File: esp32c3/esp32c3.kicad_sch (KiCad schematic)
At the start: 24 parts, among them J1 Conn_01x06, SW1 FLASH, SW2 RESET, U1 ESP32-C3-WROOM-02, U2 AHT10, U3 VEML7700, U4 LIS2DH, U5 HX6306

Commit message: add wake up, voltage measurement
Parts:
- removed C11: 10uF, Capacitor_SMD:C_0603_1608Metric, symbol Device:C_Small
- removed C3: 0.1uF, Capacitor_SMD:C_0603_1608Metric_Pad1.05x0.95mm_HandSolder, symbol e-tinkers-esp32-c3-rescue:C-Device
- removed C5: 1uF, Capacitor_SMD:C_0603_1608Metric_Pad1.05x0.95mm_HandSolder, symbol e-tinkers-esp32-c3-rescue:C-Device
- removed SW1: FLASH, e-tinkers:SW_TS-1185-X-X, symbol e-tinkers-esp32-c3-rescue:SW_Push-Switch
- added J1: A1501WR-S-2P, symbol esp32c3-altium-import:A1501WR-S-2P
- added R4: 1K, Resistor_SMD:R_0603_1608Metric_Pad1.05x0.95mm_HandSolder, symbol e-tinkers-esp32-c3-rescue:R-Device
- C4: value 0.1uF -> 10uF
- R1: value 10k -> 12k
- R5: value 12k -> 2k
- SW1: renamed from SW2; value RESET -> wake up
- renumbered J1 to J2, R4 to R6
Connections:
- net +3V3: now also R4.1; no longer R5.2
- net EN: now also J2.6 (Pin_6); no longer SW1.2
- net GND: now also R5.2
- net IO1: now also U4.6 (INT1)
- net IO2: now also R5.1, R4.2
- net IO4: now also SW1.2
- net IO10: no longer names the net of U1.10 (IO10)
- net IO18: no longer names the net of U1.13 (IO18)
- net IO19: no longer names the net of U1.14 (IO19)
- net IO3: no longer names the net of U1.15 (IO3)
- net IO5: no longer names the net of U1.4 (IO5)
- net IO6: no longer names the net of U1.5 (IO6)
- net IO7: no longer names the net of U1.6 (IO7)
- no-connect marks 2 -> 8
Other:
- moved on the sheet: C4, R1, SW1

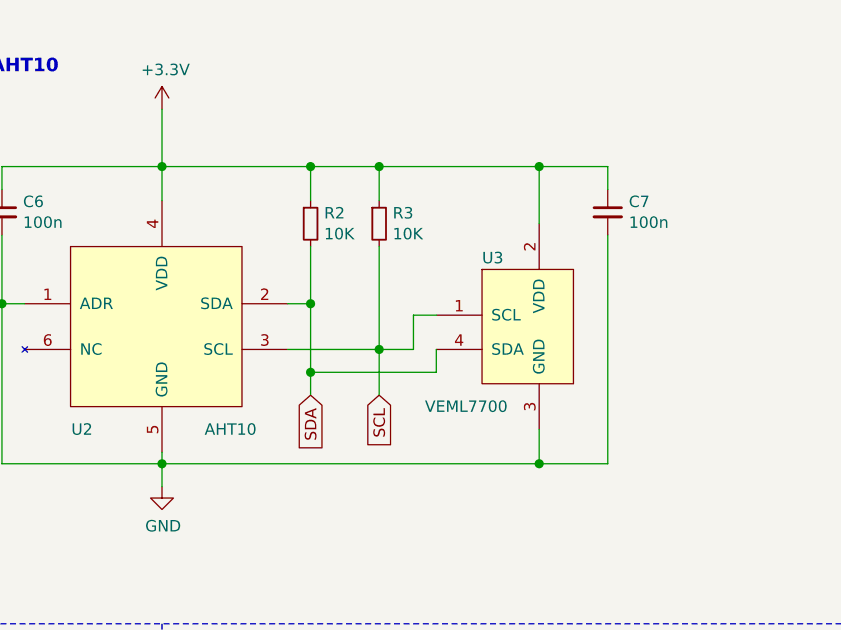
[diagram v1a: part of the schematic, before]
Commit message: delete VEML7700
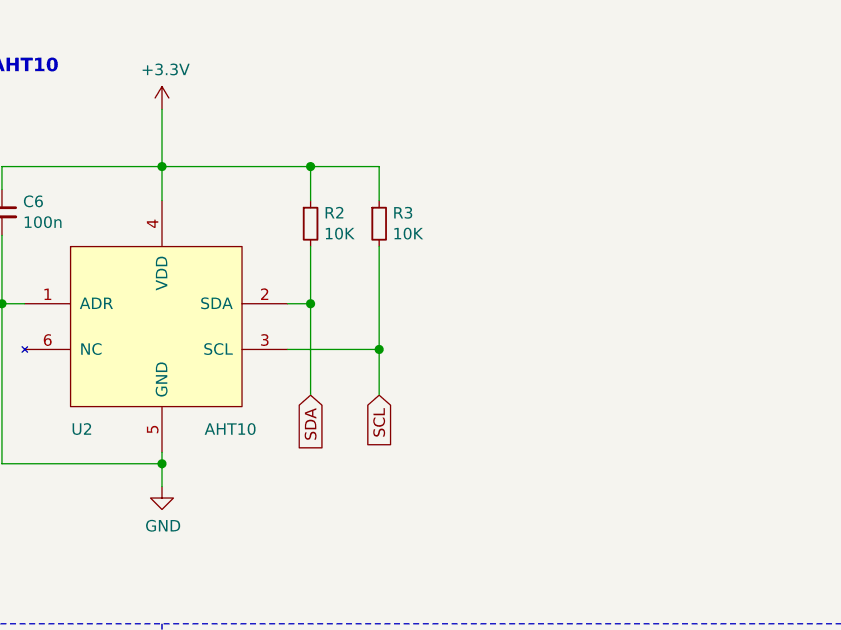
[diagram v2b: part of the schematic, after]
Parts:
- removed C7: 100n, Capacitor_SMD:C_0805_2012Metric, symbol ESP-AHT10-Extra-rescue:C_Small-Device
- removed U3: VEML7700, CPB:VEML7700, symbol ESP-AHT10-Extra-rescue:VEML7700-VEML7700
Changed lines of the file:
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@@
   (junction (at 214.63 35.56) (diameter 1.016) (color 0 0 0 0))
   (junction (at 214.63 50.8) (diameter 1.016) (color 0 0 0 0))
-  (junction (at 214.63 58.42) (diameter 1.016) (color 0 0 0 0))
-  (junction (at 222.25 35.56) (diameter 1.016) (color 0 0 0 0))
   (junction (at 222.25 55.88) (diameter 1.016) (color 0 0 0 0))
   (junction (at 231.14 118.11) (diameter 1.016) (color 0 0 0 0))
-  (junction (at 240.03 35.56) (diameter 1.016) (color 0 0 0 0))
-  (junction (at 240.03 68.58) (diameter 1.016) (color 0 0 0 0))
   (no_connect (at 25.4 49.53))
   (no_connect (at 25.4 53.34))
@@
     (stroke (width 0) (type solid) (color 0 0 0 0))
   )
-  (wire (pts (xy 198.12 68.58) (xy 240.03 68.58))
-    (stroke (width 0) (type solid) (color 0 0 0 0))
-  )
   (wire (pts (xy 212.09 50.8) (xy 214.63 50.8))
     (stroke (width 0) (type solid) (color 0 0 0 0))
@@
     (stroke (width 0) (type solid) (color 0 0 0 0))
   )
-  (wire (pts (xy 214.63 58.42) (xy 214.63 50.8))
-    (stroke (width 0) (type solid) (color 0 0 0 0))
-  )
-  (wire (pts (xy 214.63 60.96) (xy 214.63 58.42))
-    (stroke (width 0) (type solid) (color 0 0 0 0))
-  )
-  (wire (pts (xy 222.25 35.56) (xy 240.03 35.56))
+  (wire (pts (xy 214.63 50.8) (xy 214.63 60.96))
     (stroke (width 0) (type solid) (color 0 0 0 0))
   )
@@
     (stroke (width 0) (type solid) (color 0 0 0 0))
   )
-  (wire (pts (xy 226.06 52.07) (xy 226.06 55.88))
-    (stroke (width 0) (type solid) (color 0 0 0 0))
-  )
-  (wire (pts (xy 226.06 55.88) (xy 222.25 55.88))
-    (stroke (width 0) (type solid) (color 0 0 0 0))
-  )
-  (wire (pts (xy 228.6 52.07) (xy 226.06 52.07))
-    (stroke (width 0) (type solid) (color 0 0 0 0))
-  )
-  (wire (pts (xy 228.6 55.88) (xy 228.6 58.42))
-    (stroke (width 0) (type solid) (color 0 0 0 0))
-  )
-  (wire (pts (xy 228.6 58.42) (xy 214.63 58.42))
-    (stroke (width 0) (type solid) (color 0 0 0 0))
-  )
   (wire (pts (xy 231.14 115.57) (xy 231.14 118.11))
     (stroke (width 0) (type solid) (color 0 0 0 0))
@@
     (stroke (width 0) (type solid) (color 0 0 0 0))
   )
-  (wire (pts (xy 240.03 35.56) (xy 240.03 41.91))
-    (stroke (width 0) (type solid) (color 0 0 0 0))
-  )
-  (wire (pts (xy 240.03 35.56) (xy 247.65 35.56))
-    (stroke (width 0) (type solid) (color 0 0 0 0))
-  )
-  (wire (pts (xy 240.03 64.77) (xy 240.03 68.58))
-    (stroke (width 0) (type solid) (color 0 0 0 0))
-  )
   (wire (pts (xy 243.84 120.65) (xy 246.38 120.65))
     (stroke (width 0) (type solid) (color 0 0 0 0))
   )
   (wire (pts (xy 246.38 107.95) (xy 238.76 107.95))
-    (stroke (width 0) (type solid) (color 0 0 0 0))
-  )
-  (wire (pts (xy 247.65 35.56) (xy 247.65 38.1))
-    (stroke (width 0) (type solid) (color 0 0 0 0))
-  )
-  (wire (pts (xy 247.65 43.18) (xy 247.65 68.58))
-    (stroke (width 0) (type solid) (color 0 0 0 0))
-  )
-  (wire (pts (xy 247.65 68.58) (xy 240.03 68.58))
     (stroke (width 0) (type solid) (color 0 0 0 0))
   )
@@
     )
     (property "Datasheet" "~" (id 3) (at 180.34 40.64 0)
-      (effects (font (size 1.27 1.27)) hide)
-    )
-    (pin "1")
-    (pin "2")
-  )
-  (symbol (lib_id "ESP-AHT10-Extra-rescue:C_Small-Device") (at 247.65 40.64 0) (unit 1)
-    (in_bom yes) (on_board yes)
-    (property "Reference" "C7" (id 0) (at 249.9868 39.4716 0)
-      (effects (font (size 1.27 1.27)) (justify left))
-    )
-    (property "Value" "100n" (id 1) (at 249.9868 41.783 0)
-      (effects (font (size 1.27 1.27)) (justify left))
-    )
-    (property "Footprint" "Capacitor_SMD:C_0805_2012Metric" (id 2) (at 247.65 40.64 0)
-      (effects (font (size 1.27 1.27)) hide)
-    )
-    (property "Datasheet" "~" (id 3) (at 247.65 40.64 0)
       (effects (font (size 1.27 1.27)) hide)
     )
@@
     (pin "2")
     (pin "3")
-  )
-  (symbol (lib_id "ESP-AHT10-Extra-rescue:VEML7700-VEML7700") (at 240.03 53.34 0) (unit 1)
-    (in_bom yes) (on_board yes)
-    (property "Reference" "U3" (id 0) (at 233.68 45.72 0)
-      (effects (font (size 1.27 1.27)) (justify left))
-    )
-    (property "Value" "VEML7700" (id 1) (at 227.33 62.23 0)
-      (effects (font (size 1.27 1.27)) (justify left))
-    )
-    (property "Footprint" "CPB:VEML7700" (id 2) (at 233.68 48.26 0)
-      (effects (font (size 1.27 1.27)) hide)
-    )
-    (property "Datasheet" "http://www.vishay.com/docs/84286/veml7700.pdf" (id 3) (at 236.22 45.72 0)
-      (effects (font (size 1.27 1.27)) hide)
-    )
-    (pin "1")
-    (pin "2")
-    (pin "3")
-    (pin "4")
   )
   (symbol (lib_id "Sensor_Motion:LIS2DH") (at 52.07 120.65 0) (unit 1)
@@
       (reference "C6") (unit 1) (value "100n") (footprint "Capacitor_SMD:C_0805_2012Metric")
     )
-    (path "/6ff30ed5-caef-493e-9df3-acd1c93f5c4d"
-      (reference "C7") (unit 1) (value "100n") (footprint "Capacitor_SMD:C_0805_2012Metric")
-    )
     (path "/d54d20ae-378e-4d9a-abaa-c6d5a6a40f8d"
       (reference "C8") (unit 1) (value "100nF") (footprint "Capacitor_SMD:C_0603_1608Metric")
@@
       (reference "U2") (unit 1) (value "AHT10") (footprint "CPB:AHT10-HandSolder")
     )
-    (path "/770bef8b-c37f-4e6f-881f-89949b30ffb9"
-      (reference "U3") (unit 1) (value "VEML7700") (footprint "CPB:VEML7700")
-    )
     (path "/bacb6c10-c04e-42e3-94c0-aad3bde5f03c"

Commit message: finish first version of PCB
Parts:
- removed C1, C4: 10uF, Capacitor_SMD:C_0603_1608Metric_Pad1.05x0.95mm_HandSolder, symbol e-tinkers-esp32-c3-rescue:C-Device
- removed C10, C9: 1u, symbol Device:C
- removed C2: 0.1uF, Capacitor_SMD:C_0603_1608Metric_Pad1.05x0.95mm_HandSolder, symbol e-tinkers-esp32-c3-rescue:C-Device
- removed C6: 100n, Capacitor_SMD:C_0805_2012Metric, symbol ESP-AHT10-Extra-rescue:C_Small-Device
- removed C8: 100nF, Capacitor_SMD:C_0603_1608Metric, symbol Device:C_Small
- removed R1: 12k, Resistor_SMD:R_0603_1608Metric_Pad1.05x0.95mm_HandSolder, symbol e-tinkers-esp32-c3-rescue:R-Device
- removed R2, R3: 10K, Resistor_SMD:R_0805_2012Metric, symbol ESP-AHT10-Extra-rescue:R_Small-Device
- removed R4: 1K, Resistor_SMD:R_0603_1608Metric_Pad1.05x0.95mm_HandSolder, symbol e-tinkers-esp32-c3-rescue:R-Device
- removed R5: 2k, Resistor_SMD:R_0603_1608Metric_Pad1.05x0.95mm_HandSolder, symbol e-tinkers-esp32-c3-rescue:R-Device
- removed R6: 5.1k, Resistor_SMD:R_0603_1608Metric_Pad1.05x0.95mm_HandSolder, symbol e-tinkers-esp32-c3-rescue:R-Device
- added C1, C3: 10uF, Resistor_SMD:R_0603_1608Metric_Pad0.98x0.95mm_HandSolder, symbol Device:C
- added C2: 0.1uF, Resistor_SMD:R_0603_1608Metric_Pad0.98x0.95mm_HandSolder, symbol Device:C
- added C4, C5: 100nF, Resistor_SMD:R_0603_1608Metric_Pad0.98x0.95mm_HandSolder, symbol Device:C
- added C6, C7: 1uF, Resistor_SMD:R_0603_1608Metric_Pad0.98x0.95mm_HandSolder, symbol Device:C
- added D1: LED_RED, LED_SMD:LED_0805_2012Metric, symbol Device:LED_ALT
- added J3: Conn_01x05, Connector_PinSocket_2.54mm:PinSocket_1x05_P2.54mm_Vertical, symbol Connector_Generic:Conn_01x05
- added R1: 12k, Resistor_SMD:R_0603_1608Metric_Pad0.98x0.95mm_HandSolder, symbol Device:R
- added R10, R11, R12, R13, R5, R8, R9: 100k, Resistor_SMD:R_0603_1608Metric_Pad0.98x0.95mm_HandSolder, symbol Device:R
- added R2, R3, R4: 10k, Resistor_SMD:R_0603_1608Metric_Pad0.98x0.95mm_HandSolder, symbol Device:R
- added R6: 200k, Resistor_SMD:R_0603_1608Metric_Pad0.98x0.95mm_HandSolder, symbol Device:R
- added R7: 5.1k, Resistor_SMD:R_0603_1608Metric_Pad0.98x0.95mm_HandSolder, symbol Device:R
- J1: footprint (none) -> Connector_JST:JST_ZE_BM02B-ZESS-TBT_1x02-1MP_P1.50mm_Vertical
- J2: footprint (none) -> Connector_PinSocket_2.54mm:PinSocket_1x06_P2.54mm_Vertical
- SW1: footprint e-tinkers:SW_TS-1185-X-X -> Library:SW-SMD_2PIN-L4.05-W3.00-L
- U1: footprint ESP32-C3-WROOM-02:MODULE_ESP32-C3-WROOM-02 -> Library:ESP32-C3-WROOM-02
- U2: footprint CPB:AHT10-HandSolder -> Library:AHT10
- U4: renamed from U5; footprint (none) -> SOT-23
- renumbered U4 to U3
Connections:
- net +3V3: now also U3.10 (Vdd_IO), U3.2 (~CS), U3.9 (Vdd), C1.1, C2.1, C4.1, C5.1, C7.1, J3.1 (Pin_1), R1.1, R11.2, R13.2, R3.1, R4.1, R7.2, R9.2; no longer U3.4 (~CS), U3.7 (Vdd_IO), U3.8 (Vdd), U4.3 (VIN)
- net EN: now also C3.1, R1.2
- net GND: now also J1.2, U3.5 (GND), U3.6 (GND), U3.7 (GND), U3.8 (GND), C1.2, C2.2, C3.2, C4.2, C5.2, C6.2, C7.2, D1.1 (K), J3.2 (Pin_2), R10.2, R12.2, R6.2, R8.2; no longer U3.10 (GND), U3.11 (GND), U3.12 (GND), U3.13 (GND), U3.14 (GND), U3.9 (GND)
- net IO0: now also R7.1
- net IO2: now also J3.4 (Pin_4), R8.1, R9.1
- net SCL: now also U1.5 (IO6); no longer U1.8 (IO9), U2.3 (SCL)
- net SDA: now also U1.6 (IO7), U3.4 (SDA/SDI); no longer U1.7 (IO8), U2.2 (SDA), U3.2 (SDA/SDI)
- net INT: now reaches U1.10 (IO10)
- net INT: now also SW1.2
- net SCL_AHT10: now reaches U1.13 (IO18)
- net SCL_AHT10: now also U2.3 (SCL), R4.2
- net SDA_AHT10: now reaches U1.14 (IO19)
- net SDA_AHT10: now also U2.2 (SDA), R3.2
- net ADC: now reaches U1.15 (IO3)
- net ADC: now also R5.2, R6.1
- net INT1: now reaches U1.4 (IO5)
- net INT1: now also U3.12 (INT1)
- net V_In: now reaches J1.1
- net V_In: now also U4.3 (VIN), C6.1, R5.1
- net IO1 renamed LED
- net LED: now also R2.1; no longer U3.6 (INT1)
- net IO4 renamed INT2
- net INT2: now also U3.11 (INT2); no longer SW1.2
- new net: D1.2 (A), R2.2
- new net IO8: J3.5 (Pin_5), R10.1, R11.1, U1.7 (IO8)
- new net IO9: J3.3 (Pin_3), R12.1, R13.1, U1.8 (IO9)
- no-connect marks 8 -> 2
